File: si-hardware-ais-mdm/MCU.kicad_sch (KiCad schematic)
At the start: 0 parts

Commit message: added function MCU
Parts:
- added C31, C33: 104/10V, Capacitor_SMD:C_0402_1005Metric, symbol Device:C
- added C32, C35: 1uF/10V, Capacitor_SMD:C_0603_1608Metric, symbol Device:C
- added C34: 104/10V, Capacitor_SMD:C_0603_1608Metric, symbol Device:C
- added C36: 10uF/10V, Capacitor_SMD:C_0603_1608Metric, symbol Device:C
- added J4: USB_C_Receptacle_USB2.0_16P, Connector_USB:USB_C_Receptacle_G-Switch_GT-USB-7010ASV, symbol Connector:USB_C_Receptacle_USB2.0_16P
- added R15: 1K, Resistor_SMD:R_0402_1005Metric, symbol Device:R
- added R16, R19, R20: 5K1, Resistor_SMD:R_0402_1005Metric, symbol Device:R
- added R17, R18: 100, Resistor_SMD:R_0402_1005Metric, symbol Device:R
- added SW1, SW2: SW_Push, Button_Switch_SMD:SW_MEC_5GSH9, symbol Switch:SW_Push
- added U6: ESP32-C6-MINI-1-H4, ESP32-C6-MINI-1-H4:XCVR_ESP32-C6-MINI-1-H4, symbol SI_ESP32:ESP32-C6-MINI-1-H4
- added U7: LIS331HH, Package_LGA:LGA-16_3x3mm_P0.5mm_LayoutBorder3x5y, symbol Sensor_Motion:LIS331HH
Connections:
- new net: J4.B5 (CC2), R20.1
- new net: J4.A5 (CC1), R19.1
- new net: R17.1, U6.18 (IO13)
- new net: C31.1, R15.1, R16.1, SW1.2
- new net: C32.2, R15.2, U6.8 (EN)
- new net: C33.1, SW2.2, U6.23 (IO9)
- new net: U7.10 (GND), U7.12 (GND), U7.13 (GND), U7.16 (GND), U7.5 (GND)
- new net: U7.14 (Vdd), U7.15 (Vdd)
- new net: R18.1, U6.17 (IO12)
- new net: U6.21 (NC), U6.32 (NC), U6.33 (NC), U6.34 (NC), U6.35 (NC), U6.4 (NC), U6.7 (NC)
- new net +3.3V: C34.2, C35.2, C36.2, R16.2
- new net D+: J4.A6 (D+), J4.B6 (D+), R17.2
- new net D-: J4.A7 (D-), J4.B7 (D-), R18.2
- new net GND: C31.2, C32.1, C33.2, C34.1, C35.1, C36.1, J4.A1 (GND), J4.A12 (GND), J4.B1 (GND), J4.B12 (GND), J4.S1 (SHIELD), R19.2, R20.2, SW1.1, SW2.1, U6.1 (GND1), U6.11 (GND1), U6.14 (GND1), U6.2 (GND1), U6.36 (GND1), U6.37 (GND1), U6.38 (GND1), U6.39 (GND1), U6.40 (GND1), U6.41 (GND1), U6.42 (GND1), U6.43 (GND1), U6.44 (GND1), U6.45 (GND1), U6.46 (GND1), U6.47 (GND2), U6.48 (GND2), U6.49_1 (GND2), U6.49_2 (GND2), U6.49_3 (GND2), U6.49_4 (GND2), U6.49_5 (GND2), U6.49_6 (GND2), U6.49_7 (GND2), U6.49_8 (GND2), U6.49_9 (GND2), U6.50 (GND2), U6.51 (GND2), U6.52 (GND2), U6.53 (GND2)
- new net SCL: U6.24 (IO18)
- new net SDA: U6.25 (IO19)
- new net VD: J4.A4 (VBUS), J4.A9 (VBUS), J4.B4 (VBUS), J4.B9 (VBUS)
- new net mdm.CTS1: U6.26 (IO20)
- new net mdm.CTS2: U6.12 (IO0)
- new net mdm.GP1: U6.22 (IO8)
- new net mdm.GP2: U6.13 (IO1)
- new net mdm.IRQ2: U6.6 (IO3)
- new net mdm.MISO: U6.29 (IO23)
- new net mdm.MOSI: U6.28 (IO22)
- new net mdm.NSS2: U6.5 (IO2)
- new net mdm.RXCLK1: U6.16 (IO7)
- new net mdm.RXCLK2: U6.10 (IO5)
- new net mdm.RXDATA1: U6.15 (IO6)
- new net mdm.RXDATA2: U6.9 (IO4)
- new net mdm.SCLK: U6.27 (IO21)
- new net mdm.SDN1: U6.30 (RXD0)
- new net mdm.SDN2: U6.31 (TXD0)

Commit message: schematic  to pcb
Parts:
- added C37, C38: 10uF/10V, Capacitor_SMD:C_0603_1608Metric, symbol Device:C
- added R21, R22: 5K1, Resistor_SMD:R_0402_1005Metric, symbol Device:R
- SW1, SW2: footprint Button_Switch_SMD:SW_MEC_5GSH9 -> Button_Switch_SMD:SW_Tactile_SPST_NO_Straight_CK_PTS636Sx25SMTRLFS
- U6: footprint ESP32-C6-MINI-1-H4:XCVR_ESP32-C6-MINI-1-H4 -> SL_ESP:XCVR_ESP32-C6-MINI-1-H4
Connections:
- net +3.3V: now also U6.3 (3V3), U7.1 (Vdd_IO), U7.14 (Vdd), U7.15 (Vdd), C37.2, C38.2, R21.1, R22.1
- net GND: now also U7.10 (GND), U7.12 (GND), U7.13 (GND), U7.16 (GND), U7.5 (GND), C37.1, C38.1
- net SCL: now also U7.4 (SCL/SPC)
- net SDA: now also U7.6 (SDA/SDI)
- net at U7.7 (SA0/SDO): now also R21.2
- net at U7.8 (~{CS}): now also R22.2
- no-connect marks 0 -> 2

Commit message: layout and routing
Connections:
- net mdm.IRQ1: now also U6.20 (IO15)
- net mdm.NSS1: now also U6.19 (IO14)
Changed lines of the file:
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@@
+		)
+	)
+	(label "mdm.IRQ1"
+		(at 168.91 83.82 0)
+		(fields_autoplaced yes)
+		(effects
+			(font
+				(size 1.27 1.27)
+			)
+			(justify left bottom)
 		)
 	)
@@
 		(fields_autoplaced yes)
 		(effects
+			(font
+				(size 1.27 1.27)
+			)
+			(justify left bottom)
+		)
+	)
+	(label "mdm.NSS1"
+		(at 168.91 81.28 0)
+		(fields_autoplaced yes)
+		(effects

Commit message: routing 3
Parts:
- added TP1, TP2: TestPoint, TestPoint:TestPoint_Pad_D1.0mm, symbol Connector:TestPoint
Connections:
- net mdm.SDN1: now also TP2.1
- net mdm.SDN2: now also TP1.1
- net i+: now reaches R17.1, U6.18 (IO13)
- net i-: now reaches R18.1, U6.17 (IO12)
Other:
- moved on the sheet: R17, R18
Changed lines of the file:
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@@
 		)
 	)
-	(wire
-		(pts
-			(xy 125.73 91.44) (xy 138.43 91.44)
-		)
-		(stroke
-			(width 0)
-			(type default)
-		)
-	)
 	(bus
 		(pts
@@
 	(wire
 		(pts
-			(xy 125.73 93.98) (xy 138.43 93.98)
-		)
-		(stroke
-			(width 0)
-			(type default)
-		)
-	)
-	(wire
-		(pts
 			(xy 95.25 57.15) (xy 95.25 60.96)
 		)
@@
 	(wire
 		(pts
-			(xy 125.73 88.9) (xy 138.43 88.9)
+			(xy 125.73 139.7) (xy 140.97 139.7)
 		)
 		(stroke
@@
 	(wire
 		(pts
-			(xy 125.73 139.7) (xy 140.97 139.7)
+			(xy 125.73 88.9) (xy 138.43 88.9)
 		)
 		(stroke
@@
 		)
 	)
+	(wire
+		(pts
+			(xy 125.73 93.98) (xy 138.43 93.98)
+		)
+		(stroke
+			(width 0)
+			(type default)
+		)
+	)
 	(bus
 		(pts
@@
 	(wire
 		(pts
-			(xy 168.91 76.2) (xy 170.18 76.2)
+			(xy 168.91 76.2) (xy 179.07 76.2)
+		)
+		(stroke
+			(width 0)
+			(type default)
+		)
+	)
+	(wire
+		(pts
+			(xy 125.73 91.44) (xy 138.43 91.44)
 		)
 		(stroke
@@
 	(wire
 		(pts
+			(xy 168.91 71.12) (xy 184.15 71.12)
+		)
+		(stroke
+			(width 0)
+			(type default)
+		)
+	)
+	(wire
+		(pts
 			(xy 228.6 67.31) (xy 232.41 67.31)
 		)
@@
 	(wire
 		(pts
+			(xy 125.73 86.36) (xy 138.43 86.36)
+		)
+		(stroke
+			(width 0)
+			(type default)
+		)
+	)
+	(wire
+		(pts
 			(xy 72.39 125.73) (xy 88.9 125.73)
 		)
@@
 	(wire
 		(pts
-			(xy 125.73 86.36) (xy 138.43 86.36)
+			(xy 125.73 96.52) (xy 138.43 96.52)
 		)
 		(stroke
@@
 	(wire
 		(pts
-			(xy 125.73 96.52) (xy 138.43 96.52)
+			(xy 168.91 68.58) (xy 184.15 68.58)
 		)
 		(stroke
@@
 	(wire
 		(pts
-			(xy 168.91 78.74) (xy 170.18 78.74)
+			(xy 168.91 78.74) (xy 179.07 78.74)
 		)
 		(stroke
@@
 	(wire
 		(pts
-			(xy 177.8 78.74) (xy 180.34 78.74)
+			(xy 186.69 78.74) (xy 189.23 78.74)
 		)
 		(stroke
@@
 	(wire
 		(pts
-			(xy 177.8 76.2) (xy 180.34 76.2)
+			(xy 186.69 76.2) (xy 189.23 76.2)
 		)
 		(stroke
@@
 	(global_label "D-"
 		(shape input)
-		(at 180.34 76.2 0)
+		(at 189.23 76.2 0)
 		(fields_autoplaced yes)
 		(effects
@@
 		)
 		(property "Intersheetrefs" "${INTERSHEET_REFS}"
-			(at 186.1676 76.2 0)
+			(at 195.0576 76.2 0)
 			(effects
 				(font
@@
 		)
 	)
+	(global_label "i-"
+		(shape input)
+		(at 172.72 76.2 90)
+		(fields_autoplaced yes)
+		(effects
+			(font
+				(size 1.27 1.27)
+			)
+			(justify left)
+		)
+		(property "Intersheetrefs" "${INTERSHEET_REFS}"
+			(at 172.72 71.0376 90)
+			(effects
+				(font
+					(size 1.27 1.27)
+				)
+				(justify left)
+				(hide yes)
+			)
+		)
+	)
 	(global_label "SCL"
 		(shape input)
@@
 		)
 	)
+	(global_label "i+"
+		(shape input)
+		(at 175.26 78.74 90)
+		(fields_autoplaced yes)
+		(effects
+			(font
+				(size 1.27 1.27)
+			)
+			(justify left)
+		)
+		(property "Intersheetrefs" "${INTERSHEET_REFS}"
+			(at 175.26 73.5776 90)
+			(effects
+				(font
+					(size 1.27 1.27)
+				)
+				(justify left)
+				(hide yes)
+			)
+		)
+	)
 	(global_label "D+"
 		(shape input)
@@
 	(global_label "D+"
 		(shape input)
-		(at 180.34 78.74 0)
+		(at 189.23 78.74 0)
 		(fields_autoplaced yes)
 		(effects
@@
 		)
 		(property "Intersheetrefs" "${INTERSHEET_REFS}"
-			(at 186.1676 78.74 0)
+			(at 195.0576 78.74 0)
 			(effects
 				(font
@@
 	)
 	(symbol
+		(lib_id "Connector:TestPoint")
+		(at 184.15 68.58 0)
+		(unit 1)
+		(exclude_from_sim no)
+		(in_bom yes)
+		(on_board yes)
+		(dnp no)
+		(fields_autoplaced yes)
+		(property "Reference" "TP1"
+			(at 186.69 64.0079 0)
+			(effects
+				(font
+					(size 1.27 1.27)
+				)
+				(justify left)
+			)
+		)
+		(property "Value" "TestPoint"
+			(at 186.69 66.5479 0)
+			(effects
+				(font
+					(size 1.27 1.27)
+				)
+				(justify left)
+			)
+		)
+		(property "Footprint" "TestPoint:TestPoint_Pad_D1.0mm"
+			(at 189.23 68.58 0)
+			(effects
+				(font
+					(size 1.27 1.27)
+				)
+				(hide yes)
+			)
+		)
+		(property "Datasheet" "~"
+			(at 189.23 68.58 0)
+			(effects
+				(font
+					(size 1.27 1.27)
+				)
+				(hide yes)
+			)
+		)
+		(property "Description" "test point"
+			(at 184.15 68.58 0)
+			(effects
+				(font
+					(size 1.27 1.27)
+				)
+				(hide yes)
+			)
+		)
+		(pin "1"
+		)
+		(instances
+			(project ""
+				(path "/97f80214-d5cc-4a35-9cac-bb1ff8330c6a/487f8325-78ac-466b-85b4-df92bc0f13d9"
+					(reference "TP1")
+					(unit 1)
+				)
+			)
+		)
+	)
+	(symbol
 		(lib_id "power:+3.3V")
 		(at 35.56 130.81 0)
@@
 	(symbol
 		(lib_id "Device:R")
-		(at 173.99 78.74 90)
+		(at 182.88 78.74 90)
 		(unit 1)
 		(exclude_from_sim no)
@@
 		(dnp no)
 		(property "Reference" "R17"
-			(at 176.784 80.772 90)
+			(at 185.674 80.772 90)
 			(effects
 				(font
@@
 		)
 		(property "Value" "100"
-			(at 175.768 78.74 90)
+			(at 184.658 78.74 90)
 			(effects
 				(font
@@
 		)
 		(property "Footprint" "Resistor_SMD:R_0402_1005Metric"
-			(at 173.99 80.518 90)
+			(at 182.88 80.518 90)
 			(effects
 				(font
@@
 		)
 		(property "Datasheet" "~"
-			(at 173.99 78.74 0)
+			(at 182.88 78.74 0)
 			(effects
 				(font
@@
 		)
 		(property "Description" "Resistor"
-			(at 173.99 78.74 0)
+			(at 182.88 78.74 0)
 			(effects
 				(font
@@
 	)
 	(symbol
+		(lib_id "Connector:TestPoint")
+		(at 184.15 71.12 270)
+		(unit 1)
+		(exclude_from_sim no)
+		(in_bom yes)
+		(on_board yes)
+		(dnp no)
+		(fields_autoplaced yes)
+		(property "Reference" "TP2"
+			(at 189.23 69.8499 90)
+			(effects
+				(font
+					(size 1.27 1.27)
+				)
+				(justify left)
+			)
+		)
+		(property "Value" "TestPoint"
+			(at 189.23 72.3899 90)
+			(effects
+				(font
+					(size 1.27 1.27)
+				)
+				(justify left)
+			)
+		)
+		(property "Footprint" "TestPoint:TestPoint_Pad_D1.0mm"
+			(at 184.15 76.2 0)
+			(effects
+				(font
+					(size 1.27 1.27)
+				)
+				(hide yes)
+			)
+		)
+		(property "Datasheet" "~"
+			(at 184.15 76.2 0)
+			(effects
+				(font
+					(size 1.27 1.27)
+				)
+				(hide yes)
+			)
+		)
+		(property "Description" "test point"
+			(at 184.15 71.12 0)
+			(effects
+				(font
+					(size 1.27 1.27)
+				)
+				(hide yes)
+			)
+		)
+		(pin "1"
+		)
+		(instances
+			(project "si-hardware-ais-mdm"
+				(path "/97f80214-d5cc-4a35-9cac-bb1ff8330c6a/487f8325-78ac-466b-85b4-df92bc0f13d9"
+					(reference "TP2")
+					(unit 1)
+				)
+			)
+		)
+	)
+	(symbol
 		(lib_id "power:+3.3V")
 		(at 95.25 49.53 0)
@@
 	(symbol
 		(lib_id "Device:R")
-		(at 173.99 76.2 90)
+		(at 182.88 76.2 90)
 		(unit 1)
 		(exclude_from_sim no)
@@
 		(dnp no)
 		(property "Reference" "R18"
-			(at 176.022 73.914 90)
+			(at 184.912 73.914 90)
 			(effects
 				(font
@@
 		)
 		(property "Value" "100"
-			(at 175.768 76.2 90)
+			(at 184.658 76.2 90)
 			(effects
 				(font
@@
 		)
 		(property "Footprint" "Resistor_SMD:R_0402_1005Metric"
-			(at 173.99 77.978 90)
+			(at 182.88 77.978 90)
 			(effects
 				(font
@@
 		)
 		(property "Datasheet" "~"
-			(at 173.99 76.2 0)
+			(at 182.88 76.2 0)
 			(effects
 				(font
@@
 		)
 		(property "Description" "Resistor"
-			(at 173.99 76.2 0)
+			(at 182.88 76.2 0)
 			(effects
 				(font

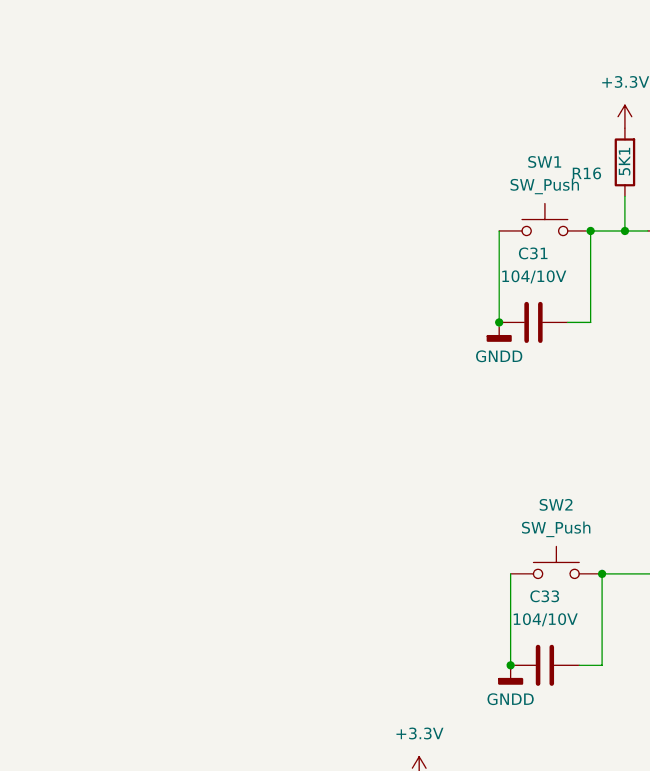
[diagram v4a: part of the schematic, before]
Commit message: added chip flash 24LC64
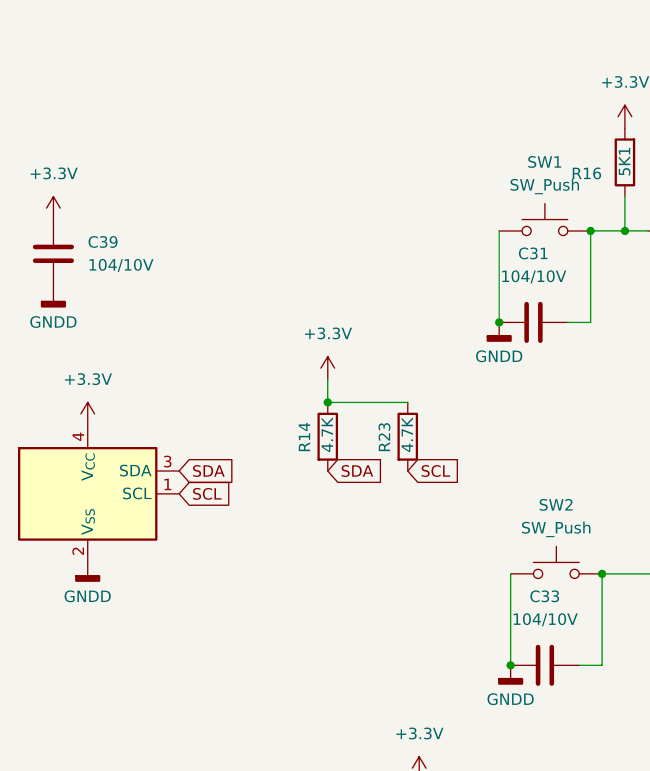
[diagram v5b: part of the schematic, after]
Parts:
- added C39: 104/10V, Capacitor_SMD:C_0402_1005Metric, symbol Device:C
- added R14, R23: 4.7K, Resistor_SMD:R_0402_1005Metric, symbol Device:R
- added U9: 24AA02E-OT, Package_TO_SOT_SMD:SOT-23-5, symbol Memory_EEPROM:24AA02E-OT
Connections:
- net +3.3V: now also C39.1, R14.1, R23.1, U9.4 (V_{CC})
- net GND: now also C39.2, U9.2 (V_{SS})
- net SCL: now also R23.2, U9.1 (SCL)
- net SDA: now also R14.2, U9.3 (SDA)

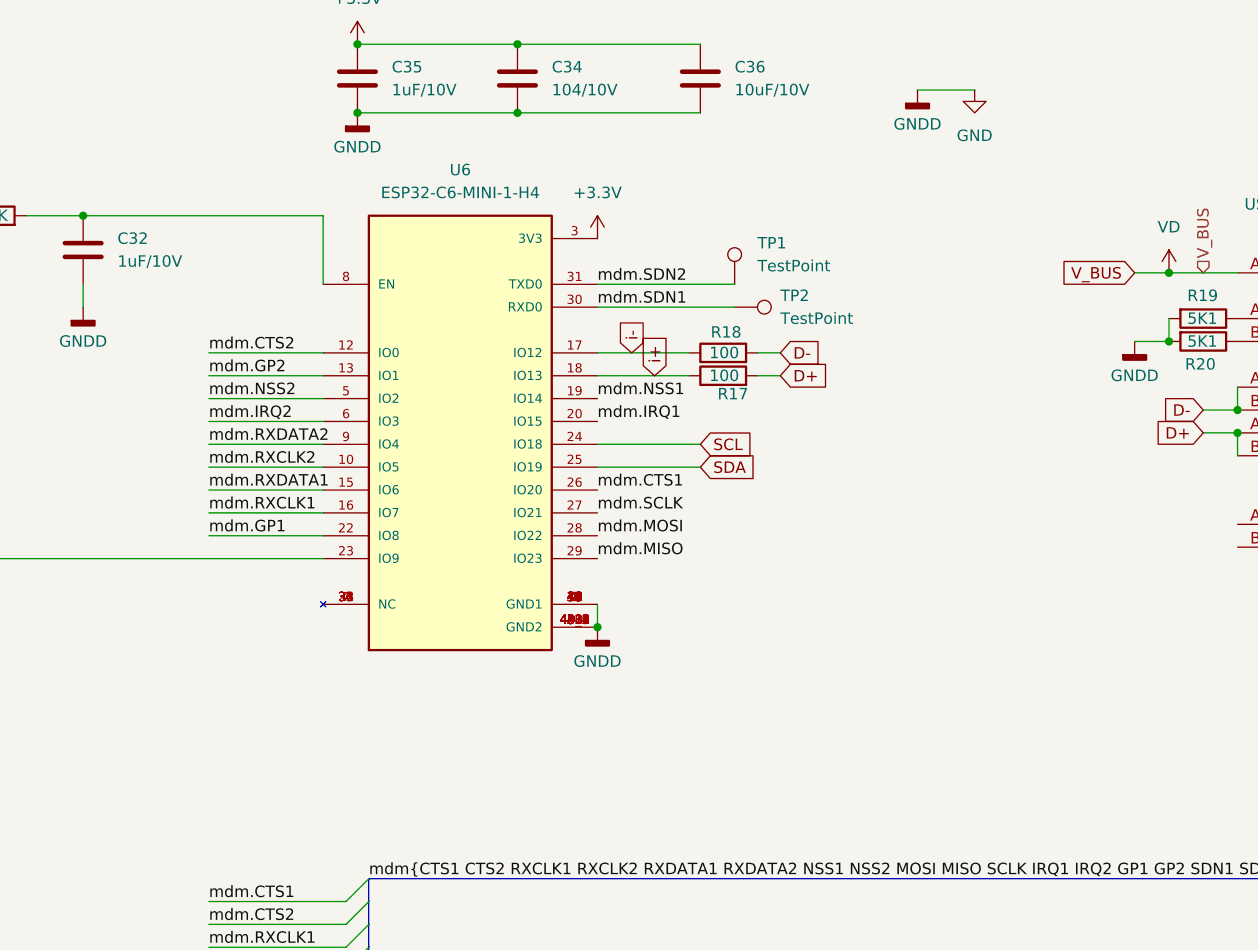
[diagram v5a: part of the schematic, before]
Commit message: added ic charger
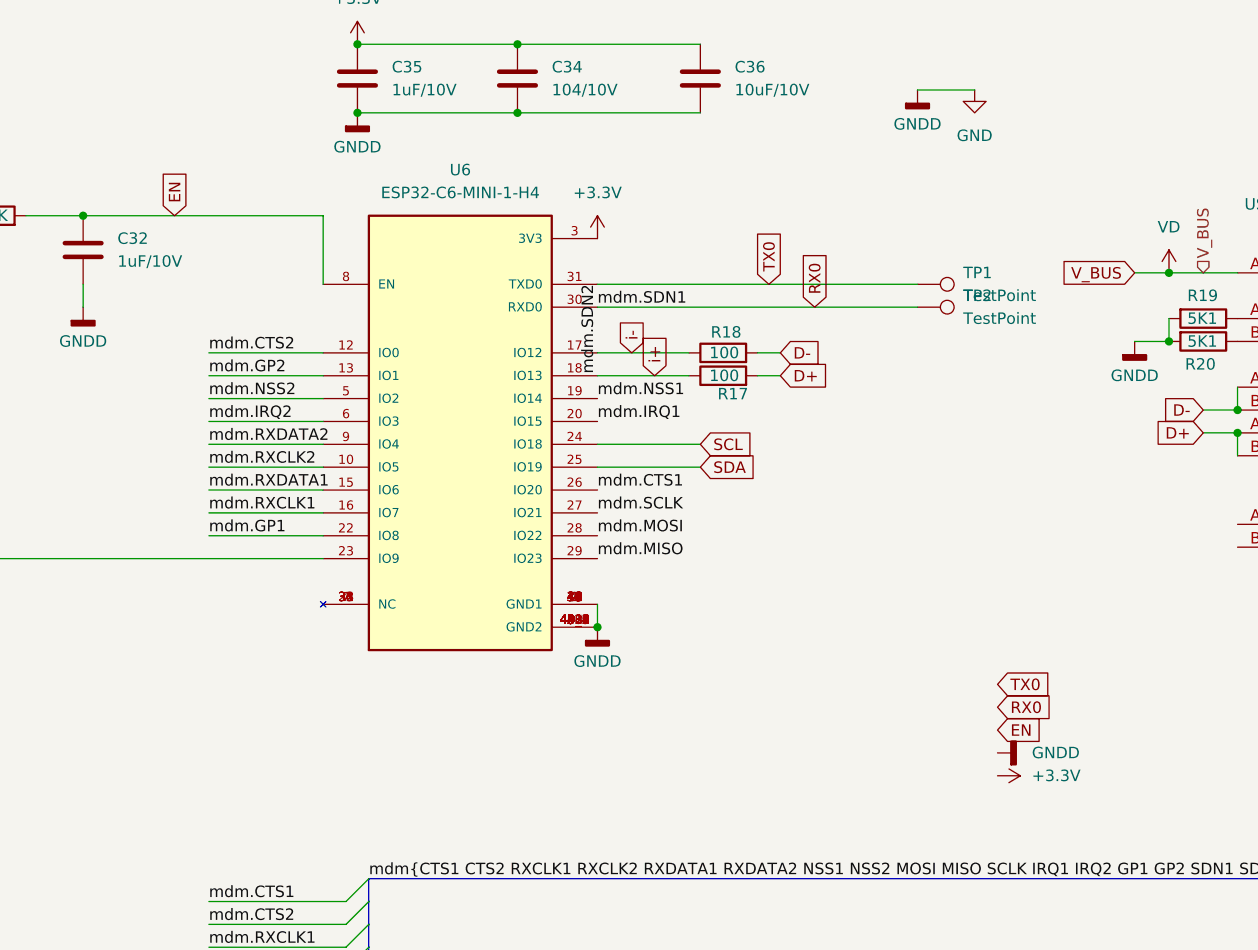
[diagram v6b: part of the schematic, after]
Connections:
- net EN: now reaches C32.2, R15.2, U6.8 (EN)
- net mdm.SDN1 renamed RX0
- net mdm.SDN2 renamed TX0
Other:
- moved on the sheet: TP1, TP2
